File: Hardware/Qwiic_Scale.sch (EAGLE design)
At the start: 32 parts, among them J1 JUMPER-SMT_2_NC_TRACE_SILK, J2 Qwiic Right Angle, J3 PTH, J4 Qwiic Right Angle, J7 Spring Terminal, U1 NAU7802

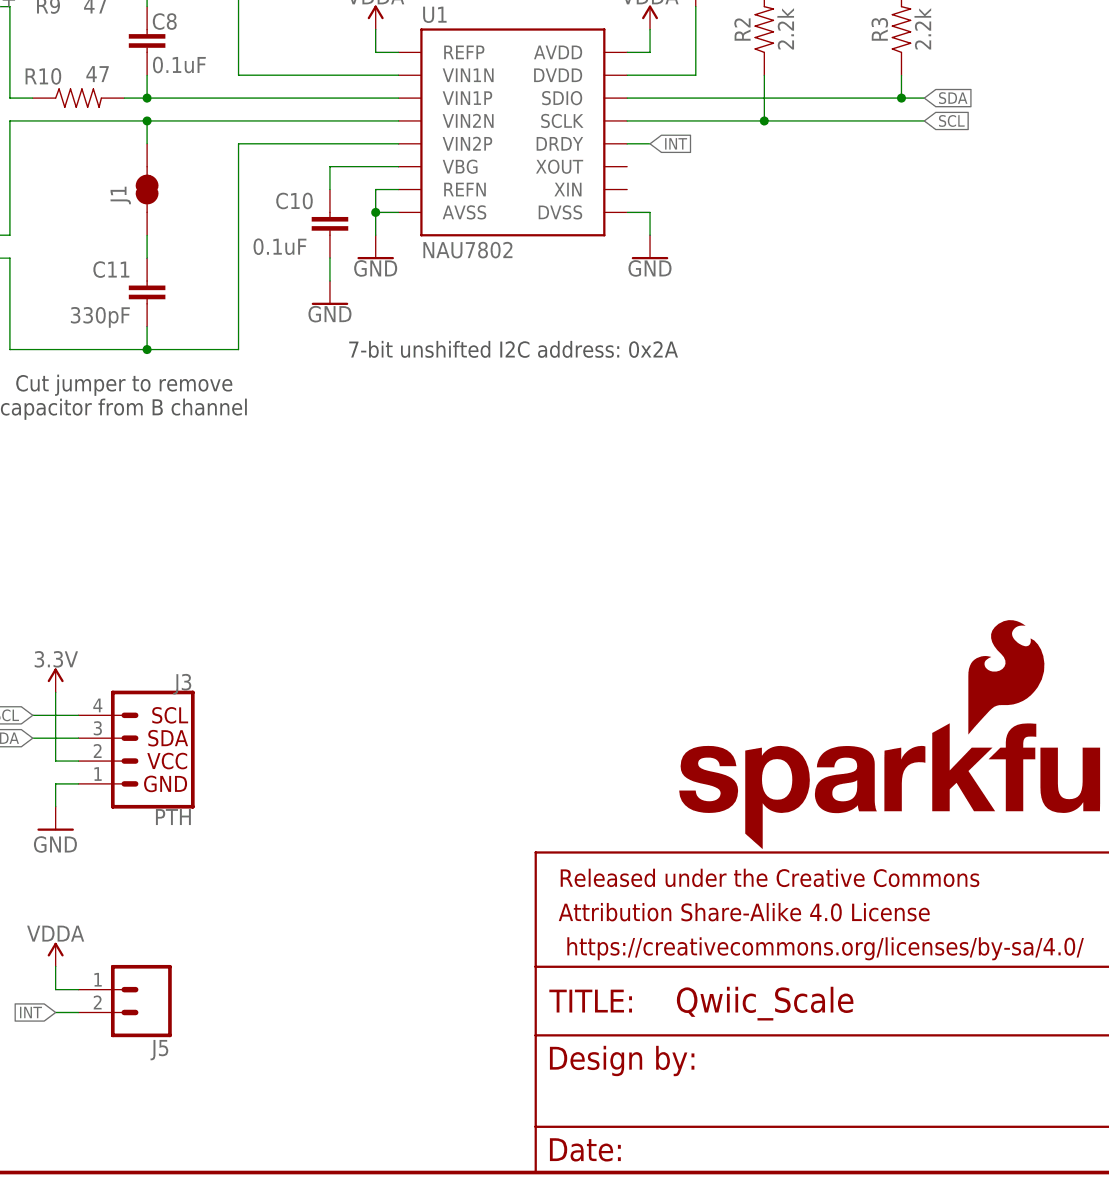
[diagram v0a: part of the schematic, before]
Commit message: Silk change to terminal. Better ground ties.
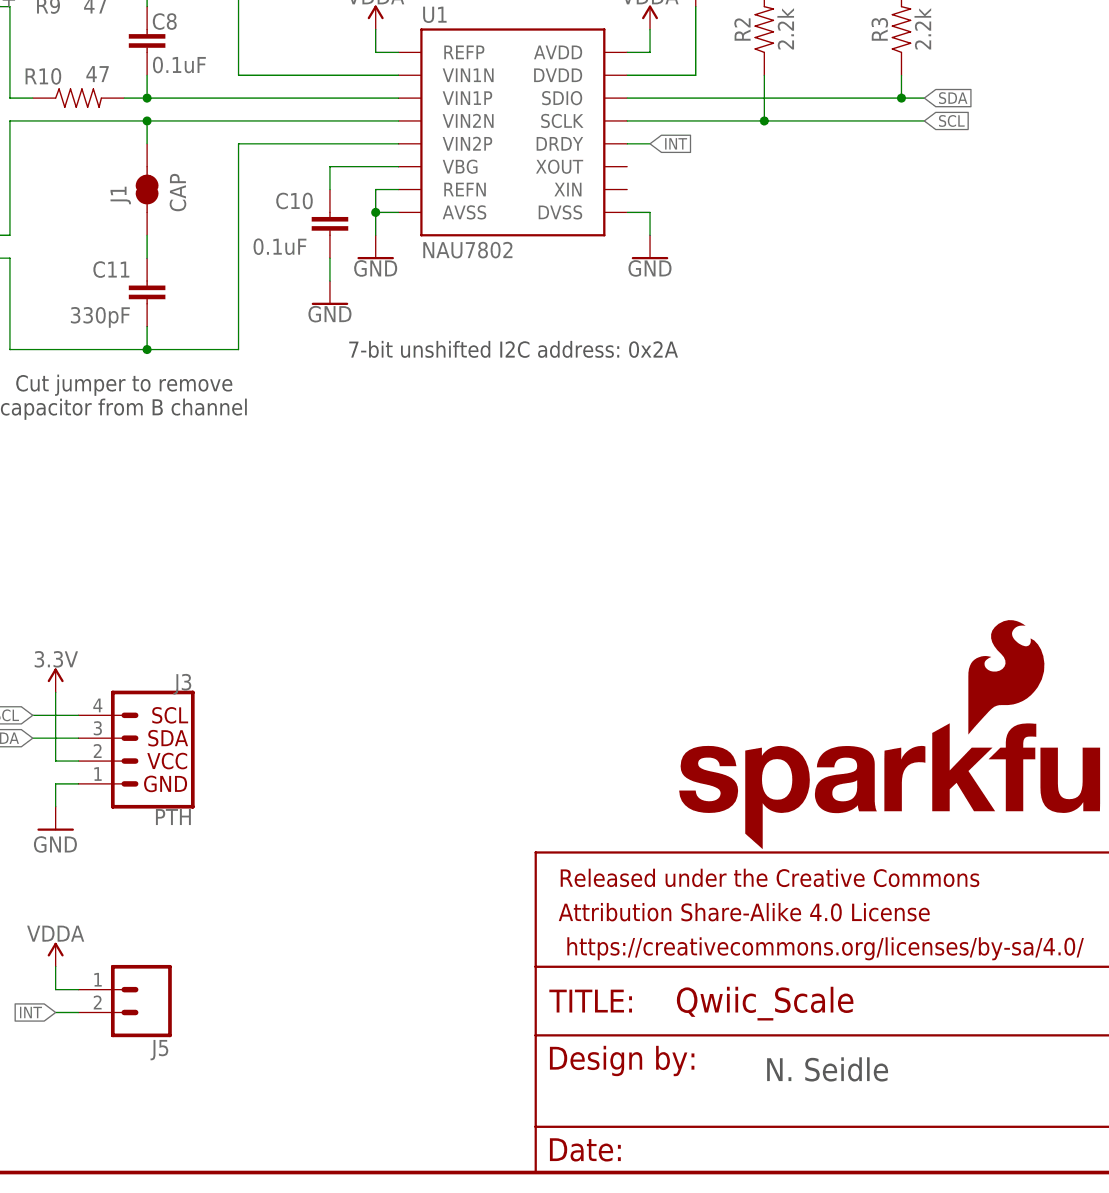
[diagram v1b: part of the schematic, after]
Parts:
- J1: value JUMPER-SMT_2_NC_TRACE_SILK -> CAP
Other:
- note added: "N. Seidle"
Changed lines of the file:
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@@
 <part name="R1" library="SparkFun-Resistors" deviceset="1KOHM" device="-0603-1/10W-1%" value="1k"/>
 <part name="U$73" library="SparkFun-PowerSymbols" deviceset="VDDA" device=""/>
-<part name="J1" library="SparkFun-Jumpers" deviceset="JUMPER-SMT_2_NC_TRACE" device="_SILK" value=""/>
+<part name="J1" library="SparkFun-Jumpers" deviceset="JUMPER-SMT_2_NC_TRACE" device="_SILK" value="CAP"/>
 <part name="J5" library="SparkFun-Connectors" deviceset="CONN_02" device="1X02_NO_SILK"/>
 <part name="U$74" library="SparkFun-PowerSymbols" deviceset="VDDA" device=""/>
@@
 <text x="101.6" y="86.36" size="1.778" layer="97" font="vector" align="center">Cut jumper to remove
 capacitor from B channel</text>
+<text x="172.72" y="10.16" size="2.54" layer="97">N. Seidle</text>
 </plain>
 <instances>

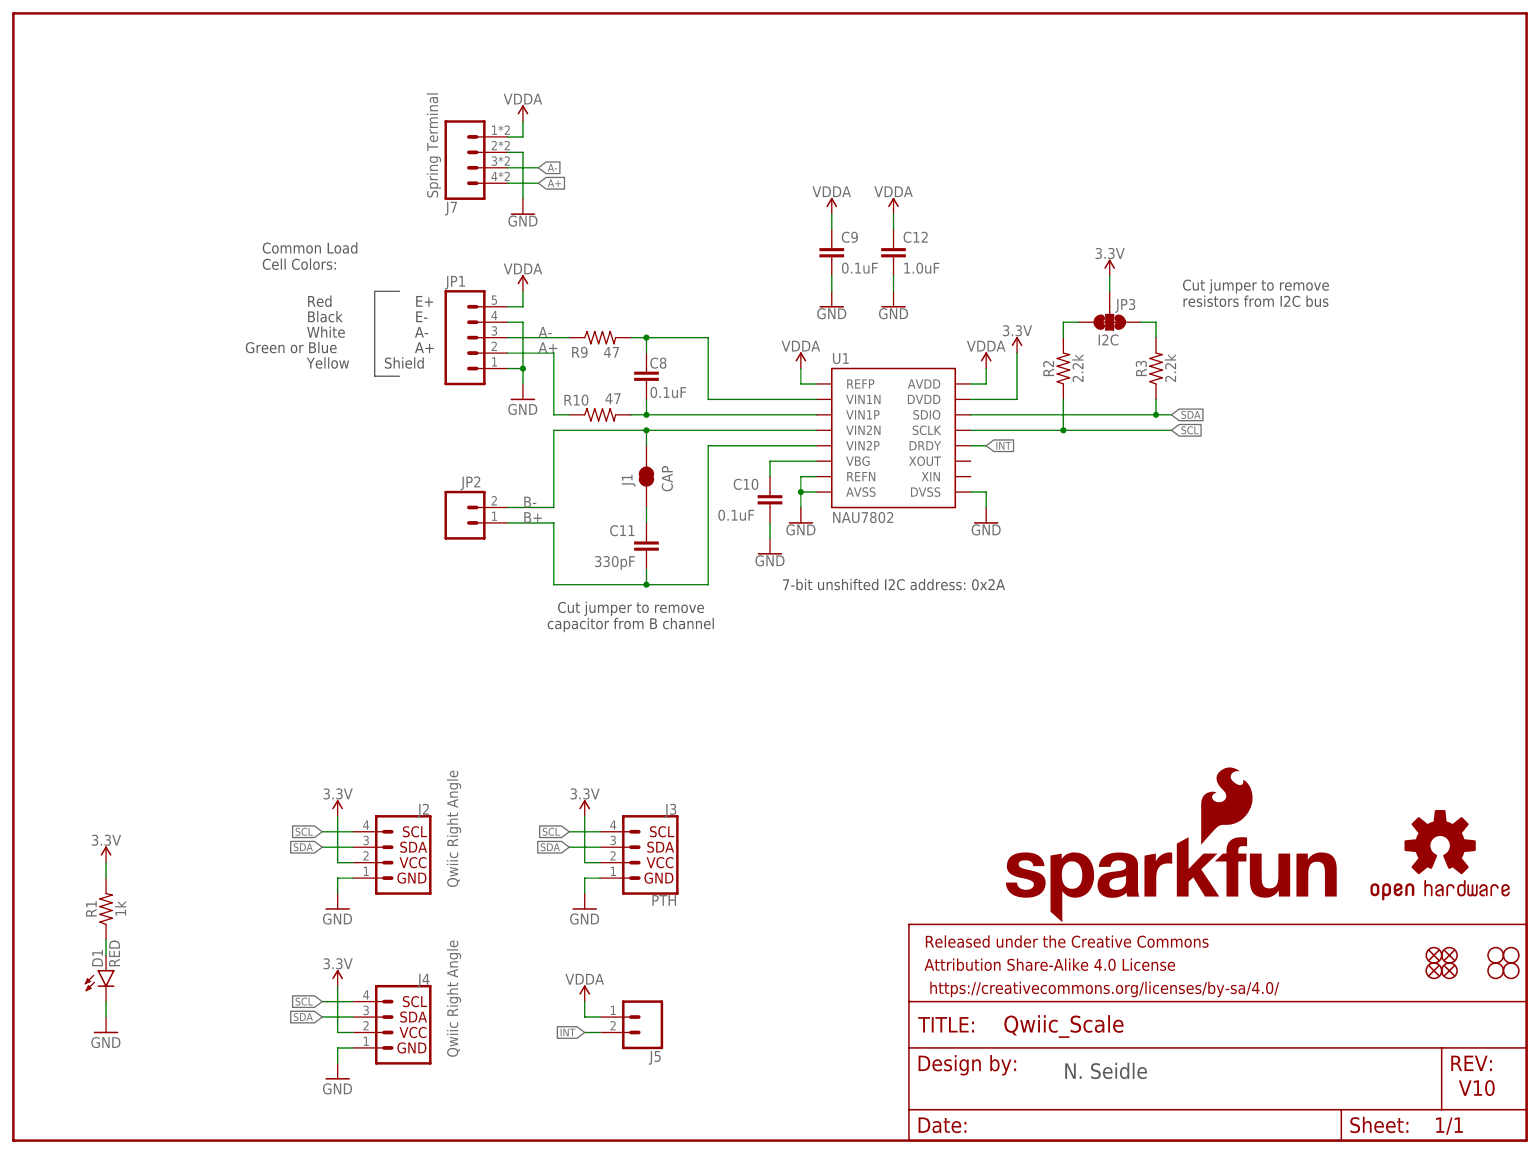
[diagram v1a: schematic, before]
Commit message: Divided schematic. Added VDD range.
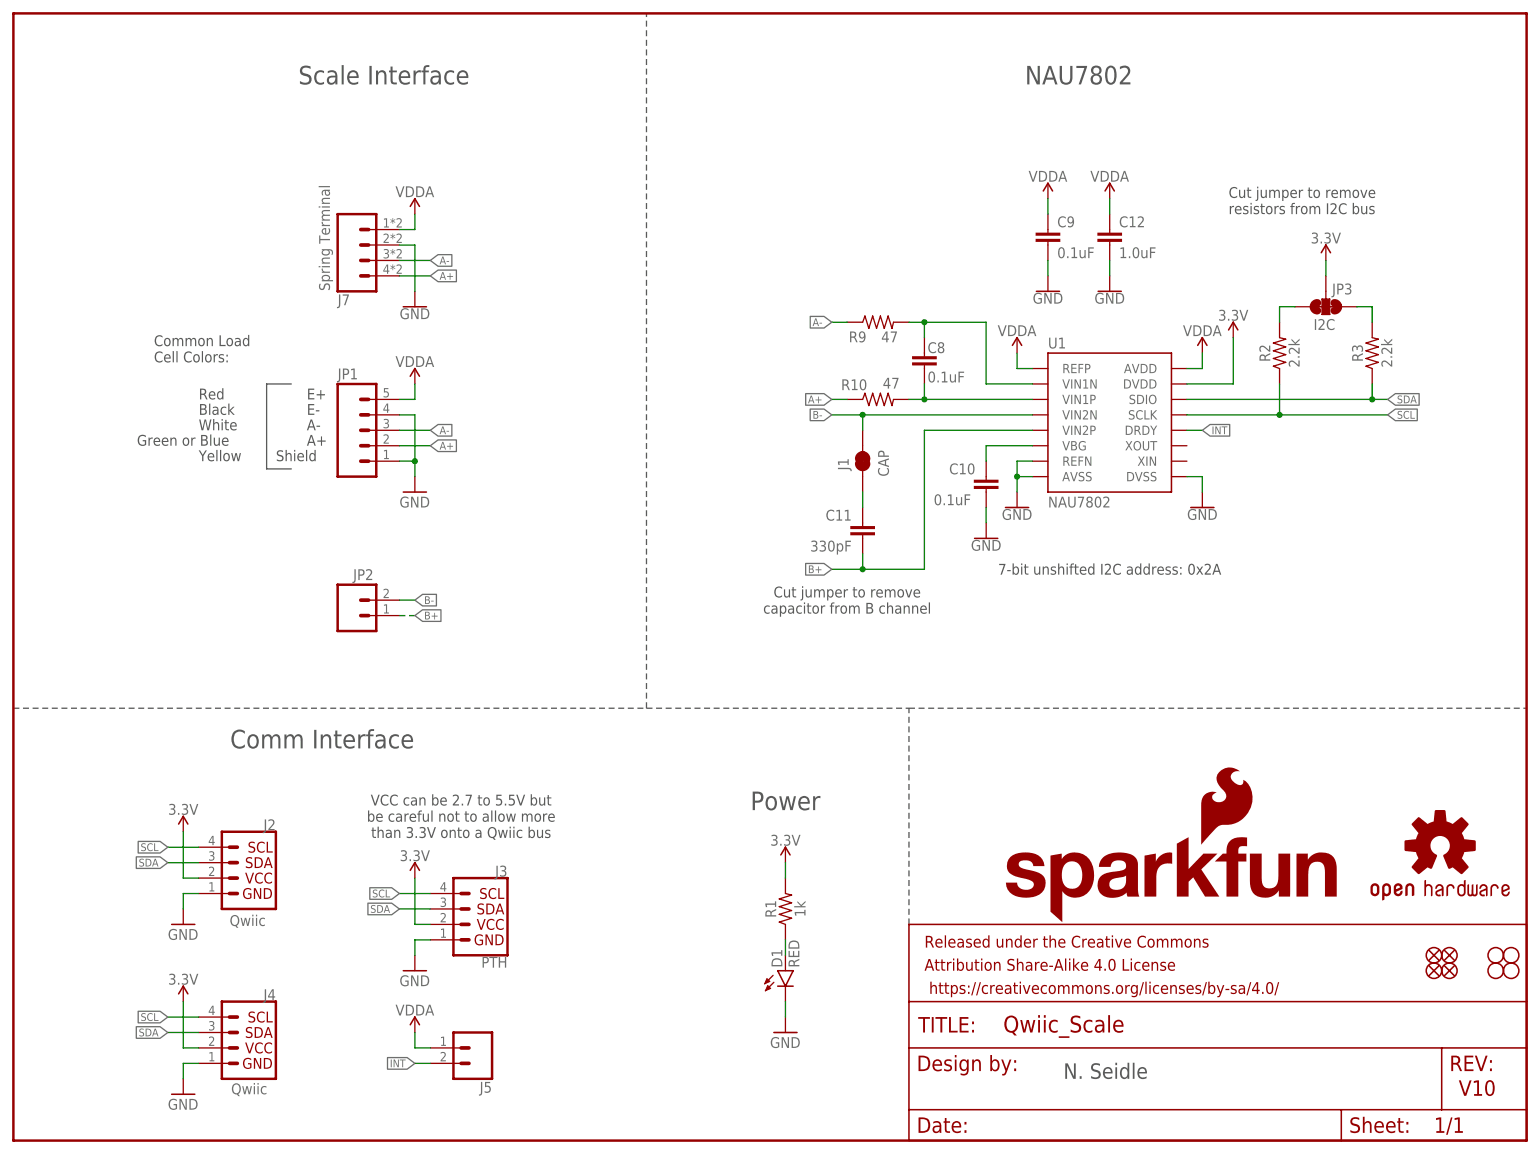
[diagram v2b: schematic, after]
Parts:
- J2, J4: value Qwiic Right Angle -> Qwiic
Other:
- note added: "Comm Interface"
- note added: "NAU7802"
- note added: "Power"
- note added: "Scale Interface"
- note added: "VCC can be 2.7 to 5.5V but be careful not to allow more than 3.3V onto a Qwiic bus"
- moved on the sheet: C10, C11, C12, C8, C9, D1, J1, J2, J3, J4, J5, J7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

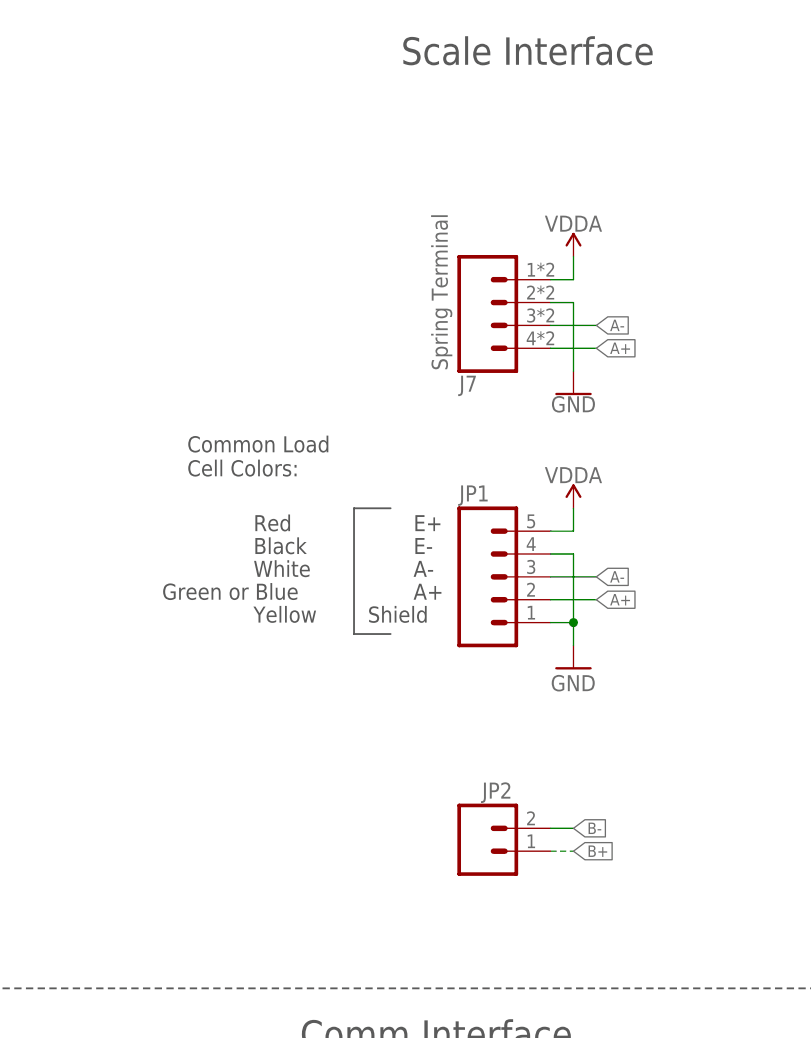
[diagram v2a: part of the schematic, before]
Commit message: Divided schematic. Added VDD range.
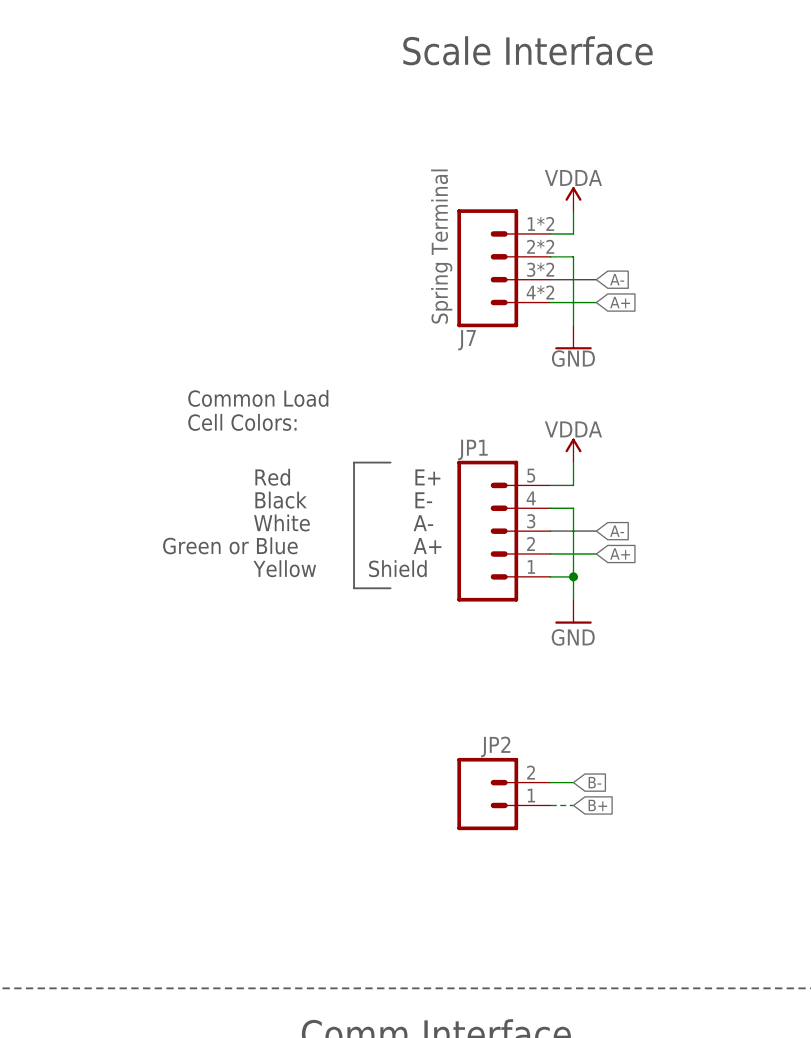
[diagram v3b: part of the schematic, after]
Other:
- moved on the sheet: J7, JP1, JP2
